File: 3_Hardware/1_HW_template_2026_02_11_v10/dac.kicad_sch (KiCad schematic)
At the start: 5 parts, among them U10 MCP6001

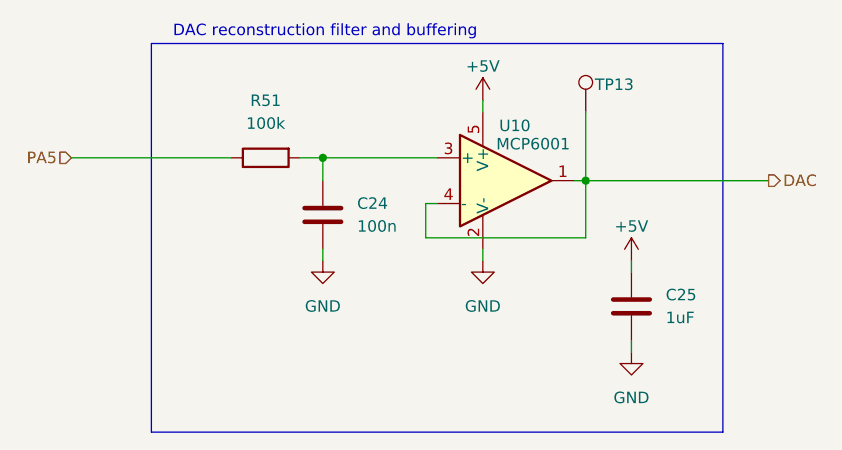
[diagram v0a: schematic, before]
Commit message: added amp filter v5
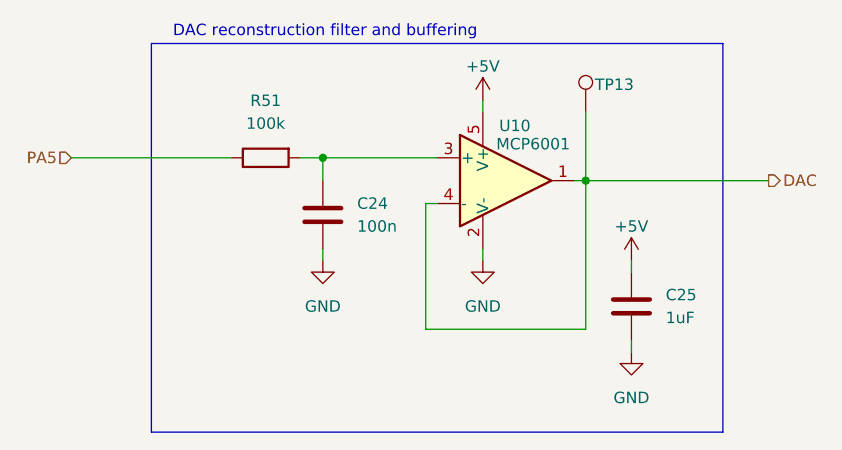
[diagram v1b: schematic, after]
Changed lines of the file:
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@@
 	(wire
 		(pts
-			(xy 148.59 95.25) (xy 148.59 88.9)
+			(xy 148.59 105.41) (xy 148.59 88.9)
 		)
 		(stroke
@@
 	(wire
 		(pts
-			(xy 130.81 91.44) (xy 130.81 95.25)
+			(xy 130.81 91.44) (xy 130.81 105.41)
 		)
 		(stroke
@@
 	(wire
 		(pts
-			(xy 130.81 95.25) (xy 148.59 95.25)
+			(xy 130.81 105.41) (xy 148.59 105.41)
 		)
 		(stroke

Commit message: finalize main feature
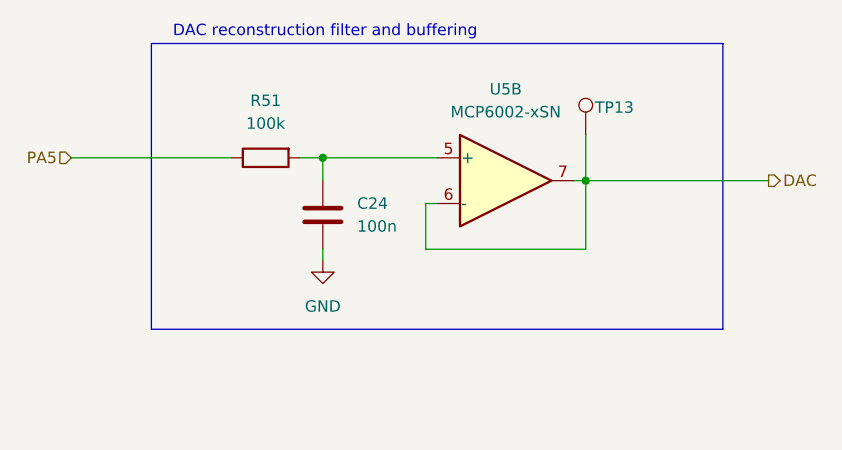
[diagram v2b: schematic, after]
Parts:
- removed C25: 1uF, Capacitor_SMD:C_0805_2012Metric_Pad1.18x1.45mm_HandSolder, symbol Device:C
- removed U10: MCP6001, Package_TO_SOT_SMD:TSOT-23-5, symbol Amplifier_Operational:AD8603
- added U5: MCP6002-xSN, Package_SO:SOIC-8_3.9x4.9mm_P1.27mm, symbol Amplifier_Operational:MCP6002-xSN
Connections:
- net DAC: now also U5.6 (-), U5.7
- net at C24.1, R51.2: now also U5.5 (+)
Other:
- moved on the sheet: TP13

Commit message: layout template
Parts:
- renumbered C24 to C19, R51 to R20, TP13 to TP6, U5 to U3
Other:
- note added: "tau = R*C = 10ms fg = ~ 16 Hz"
- moved on the sheet: C19, R20, TP6, U3B

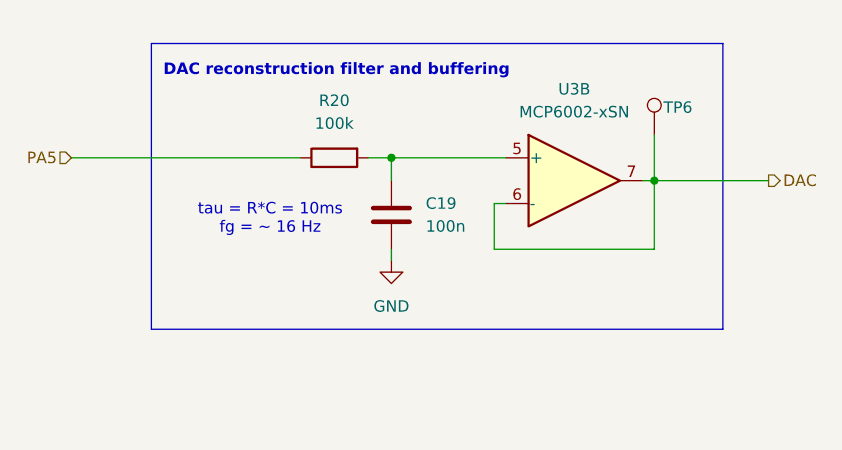
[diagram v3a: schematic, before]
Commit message: updated layout
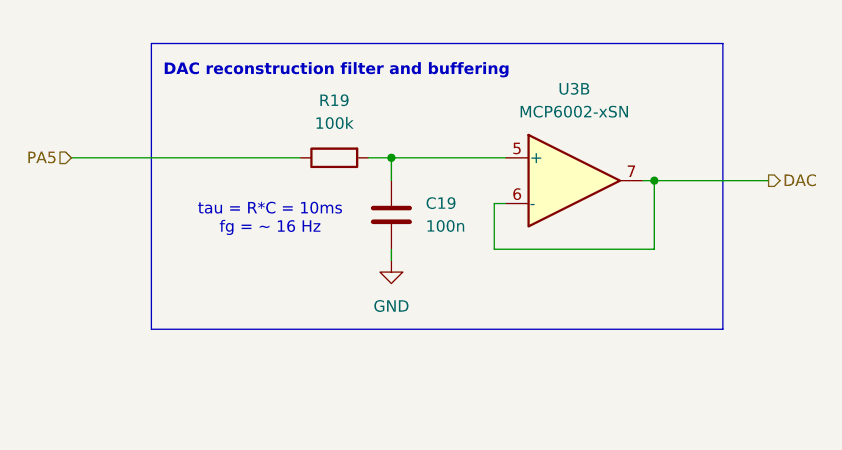
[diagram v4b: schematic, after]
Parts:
- removed TP6: ${SIM.PARAMS}, TestPoint:TestPoint_Loop_D2.60mm_Drill1.6mm_Beaded, symbol Connector:TestPoint
- renumbered R20 to R19
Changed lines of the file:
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@@
-	(wire
-		(pts
-			(xy 156.21 83.82) (xy 156.21 88.9)
-		)
-		(stroke
-			(width 0)
-			(type default)
-		)
-	)
 	(wire
 		(pts
@@
 			)
 			(justify right)
-		)
-	)
-	(symbol
-		(lib_id "Connector:TestPoint")
-		(at 156.21 83.82 0)
-		(unit 1)
-		(exclude_from_sim yes)
-		(in_bom yes)
-		(on_board yes)
-		(dnp no)
-		(property "Reference" "TP6"
-			(at 157.226 80.772 0)
-			(effects
-				(font
-					(size 1.27 1.27)
-				)
-				(justify left)
-			)
-		)
-		(property "Value" "${SIM.PARAMS}"
-			(at 158.75 81.7879 0)
-			(effects
-				(font
-					(size 1.27 1.27)
-				)
-				(justify left)
-			)
-		)
-		(property "Footprint" "TestPoint:TestPoint_Loop_D2.60mm_Drill1.6mm_Beaded"
-			(at 161.29 83.82 0)
-			(effects
-				(font
-					(size 1.27 1.27)
-				)
-				(hide yes)
-			)
-		)
-		(property "Datasheet" "~"
-			(at 161.29 83.82 0)
-			(effects
-				(font
-					(size 1.27 1.27)
-				)
-				(hide yes)
-			)
-		)
-		(property "Description" ""
-			(at 156.21 83.82 0)
-			(effects
-				(font
-					(size 1.27 1.27)
-				)
-				(hide yes)
-			)
-		)
-		(property "Sim.Device" ""
-			(at 156.21 83.82 0)
-			(effects
-				(font
-					(size 1.27 1.27)
-				)
-				(hide yes)
-			)
-		)
-		(property "Sim.Params" ""
-			(at 74.93 -40.64 0)
-			(effects
-				(font
-					(size 1.27 1.27)
-				)
-				(hide yes)
-			)
-		)
-		(property "Sim.Pins" "1=1"
-			(at 74.93 -40.64 0)
-			(effects
-				(font
-					(size 1.27 1.27)
-				)
-				(hide yes)
-			)
-		)
-		(pin "1"
-		)
-		(instances
-			(project "HW_template"
-				(path "/1f276d59-ad9b-4e70-a842-f3b7e562eb9b/b4c75508-242a-42f6-bbff-7db575bcc9ab"
-					(reference "TP6")
-					(unit 1)
-				)
-			)
 		)
 	)
@@
 		(dnp no)
 		(fields_autoplaced yes)
-		(property "Reference" "#PWR032"
+		(property "Reference" "#PWR030"
 			(at 127 104.14 0)
 			(effects
@@
 			(project "HW_template"
 				(path "/1f276d59-ad9b-4e70-a842-f3b7e562eb9b/b4c75508-242a-42f6-bbff-7db575bcc9ab"
-					(reference "#PWR032")
+					(reference "#PWR030")
 					(unit 1)
 				)
@@
 		(on_board yes)
 		(dnp no)
-		(property "Reference" "R20"
+		(property "Reference" "R19"
 			(at 120.65 80.01 90)
 			(effects
@@
 			(project "HW_template"
 				(path "/1f276d59-ad9b-4e70-a842-f3b7e562eb9b/b4c75508-242a-42f6-bbff-7db575bcc9ab"
-					(reference "R20")
+					(reference "R19")
 					(unit 1)
 				)

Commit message: fixed footprints
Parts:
- C19: footprint Capacitor_SMD:C_0805_2012Metric_Pad1.18x1.45mm_HandSolder -> Capacitor_SMD:C_0603_1608Metric_Pad1.08x0.95mm_HandSolder
- R19: footprint Resistor_SMD:R_0805_2012Metric_Pad1.20x1.40mm_HandSolder -> Resistor_SMD:R_0603_1608Metric_Pad0.98x0.95mm_HandSolder
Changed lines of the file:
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@@
 			)
 		)
-		(property "Footprint" "Capacitor_SMD:C_0805_2012Metric_Pad1.18x1.45mm_HandSolder"
+		(property "Footprint" "Capacitor_SMD:C_0603_1608Metric_Pad1.08x0.95mm_HandSolder"
 			(at 127.9652 96.52 0)
 			(effects
@@
 			)
 		)
-		(property "Footprint" "Resistor_SMD:R_0805_2012Metric_Pad1.20x1.40mm_HandSolder"
+		(property "Footprint" "Resistor_SMD:R_0603_1608Metric_Pad0.98x0.95mm_HandSolder"
 			(at 120.65 84.582 90)
 			(effects

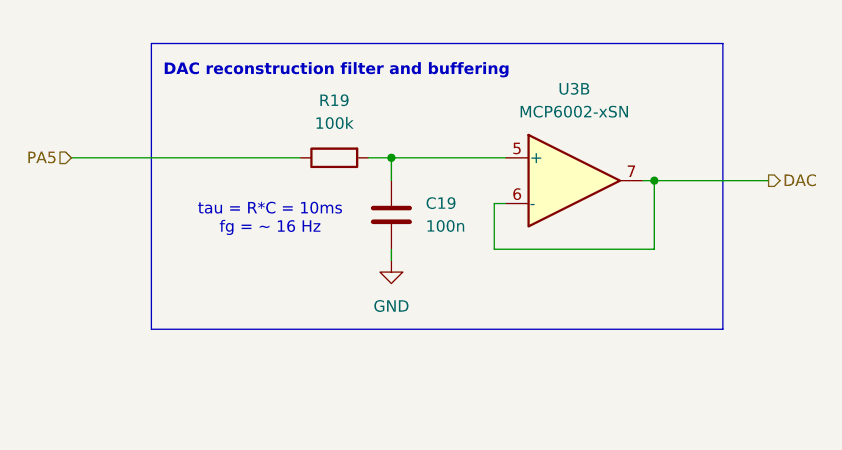
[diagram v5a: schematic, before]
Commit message: added amplification to VCO
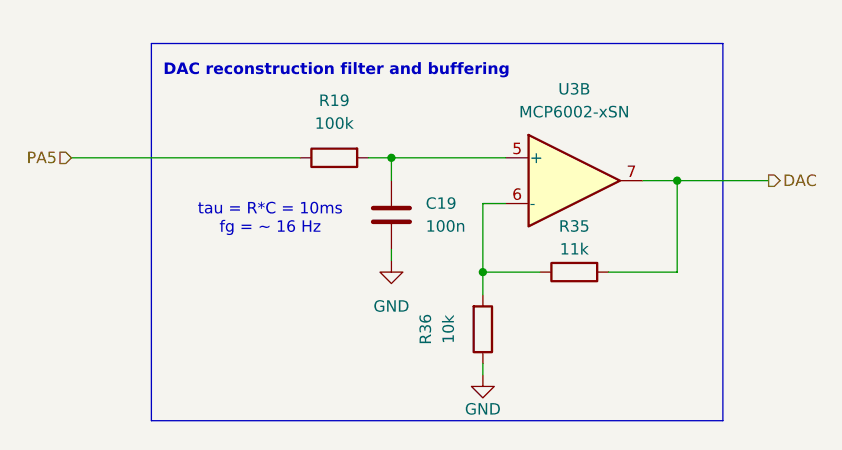
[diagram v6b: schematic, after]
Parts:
- added R35: 11k, Resistor_SMD:R_0603_1608Metric_Pad0.98x0.95mm_HandSolder, symbol Device:R
- added R36: 10k, Resistor_SMD:R_0603_1608Metric_Pad0.98x0.95mm_HandSolder, symbol Device:R
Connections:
- net DAC: now also R35.2; no longer U3.6 (-)
- net GND: now also R36.1
- new net: R35.1, R36.2, U3.6 (-)

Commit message: vco error fixed: replaced 11k with 1k
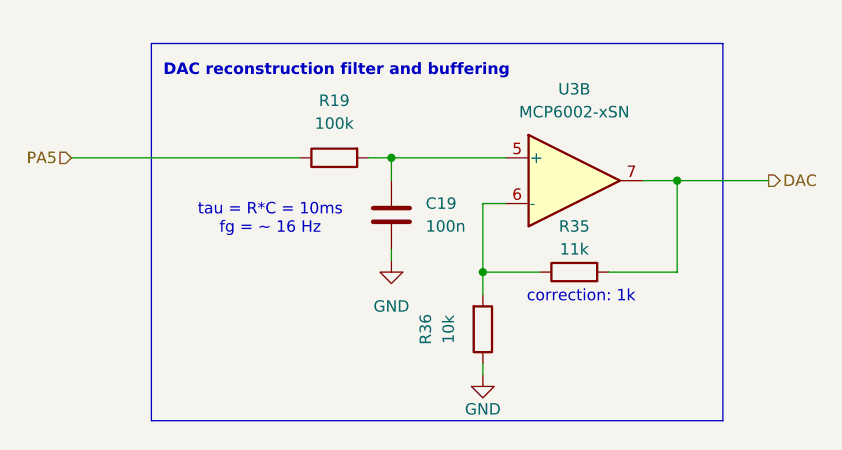
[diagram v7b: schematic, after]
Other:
- note added: "correction: 1k"
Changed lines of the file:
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@@
+		)
+	)
+	(text "correction: 1k"
+		(exclude_from_sim no)
+		(at 148.082 101.854 0)
+		(effects
+			(font
+				(size 1.27 1.27)
+				(color 255 0 0 1)
+			)
 		)
 	)
